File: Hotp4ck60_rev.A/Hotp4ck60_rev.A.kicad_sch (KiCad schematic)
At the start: 42 parts, among them Q1 2N7002, SW1 PWR, U1 nRF52840, U2 BQ24075RGT, U3 TPS7A20xxxDQN, U4 MAX17048, X1 32 MHz, X2 32.768 KHz

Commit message: 기판 아트웍 재시작
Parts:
- U2: footprint Package_DFN_QFN:VQFN-16-1EP_3x3mm_P0.5mm_EP1.6x1.6mm -> lib:VQFN-16-1EP_3x3mm_P0.5mm_EP1.6x1.6mm
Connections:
- net ~{RST}: now reaches U1.AC13 (P0.18/~{RESET})
- net ~{RST}: now also U1.AD12 (P0.17)
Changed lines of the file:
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@@
 	(wire
 		(pts
+			(xy 137.16 96.52) (xy 133.35 96.52)
+		)
+		(stroke
+			(width 0)
+			(type default)
+		)
+	)
+	(wire
+		(pts
 			(xy 222.25 119.38) (xy 223.52 119.38)
 		)
@@
 	(wire
 		(pts
+			(xy 63.5 160.02) (xy 67.31 160.02)
+		)
+		(stroke
+			(width 0)
+			(type default)
+		)
+	)
+	(wire
+		(pts
 			(xy 212.09 92.71) (xy 212.09 93.98)
 		)
@@
 		)
 	)
+	(label "~{RST}"
+		(at 63.5 160.02 0)
+		(effects
+			(font
+				(size 1.27 1.27)
+			)
+			(justify left bottom)
+		)
+	)
 	(label "~{CHG}"
 		(at 248.92 53.34 180)
@@
 		)
 	)
+	(label "~{RST}"
+		(at 137.16 96.52 180)
+		(effects
+			(font
+				(size 1.27 1.27)
+			)
+			(justify right bottom)
+		)
+	)
 	(label "XL1"
 		(at 137.16 53.34 180)
@@
 			)
 		)
-		(property "Footprint" "Package_DFN_QFN:VQFN-16-1EP_3x3mm_P0.5mm_EP1.6x1.6mm"
+		(property "Footprint" "lib:VQFN-16-1EP_3x3mm_P0.5mm_EP1.6x1.6mm"
 			(at 238.76 57.15 0)
 			(hide yes)

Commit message: 키보드 기판 소자 재배치 중
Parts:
- added AE1: ANT, RF_Antenna:Texas_SWRA117D_2.4GHz_Right, symbol Device:Antenna_Dipole
- added C24: 0.8nF, Capacitor_SMD:C_0402_1005Metric, symbol PCM_JLCPCB-Capacitors:0402,100nF,(2)
- added C25: 0.5nF, Capacitor_SMD:C_0402_1005Metric, symbol PCM_JLCPCB-Capacitors:0402,100nF,(2)
- added J1: POGO, Connector_PinHeader_2.54mm:PinHeader_1x05_P2.54mm_Vertical, symbol Connector_Generic:Conn_01x05
- added J2: ai03_unified_daughter_board, Connector_JST:JST_SH_SM04B-SRSS-TB_1x04-1MP_P1.00mm_Horizontal, symbol Connector_Generic_MountingPin:Conn_01x04_MountingPin
- added J3: Battery Connector, Connector_Molex:Molex_PicoBlade_53261-0271_1x02-1MP_P1.25mm_Horizontal, symbol Connector_Generic_MountingPin:Conn_01x02_MountingPin
- added L3: 4.7nH, 700mA, Inductor_SMD:L_0402_1005Metric, symbol Device:L_Small
- added R1: 0Ω, Resistor_SMD:R_0402_1005Metric, symbol PCM_JLCPCB-Resistors:0402,0Ω
- L1: value 10 uH, 50mA -> 10uH,50mA; Category (none) -> Inductors/Coils/Transformers,Inductors (SMD); Class (none) -> Extended Component; DC Resistance (DCR) (none) -> 900mΩ; Inductance (none) -> 10uH; LCSC (none) -> C50325679; Manufacturer (none) -> APV; Part (none) -> APQM18FN100M00D; Process (none) -> SMT; Rated Current (none) -> 50mA; Tolerance (none) -> ±20%
- L2: value 15 nH -> 15nH; Category (none) -> Inductors/Coils/Transformers,Inductors (SMD); Class (none) -> Extended Component; DC Resistance (DCR) (none) -> 500mΩ; Inductance (none) -> 15nH; LCSC (none) -> C395049; Manufacturer (none) -> FH; Part (none) -> VHF100505HQ15NJT; Process (none) -> SMT; Rated Current (none) -> 400mA; Tolerance (none) -> ±5%
- renumbered R1 to R2, R2 to R3, R3 to R4, R4 to R5
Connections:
- net +BATT: now also J1.5 (Pin_5), J3.1 (Pin_1)
- net GND: now also Q1.2 (S), R9.2, SW1.3 (C), AE1.2, C24.1, C25.1, J1.4 (Pin_4), J2.4 (Pin_4), J2.MP (MountPin), J3.2 (Pin_2), J3.MP (MountPin), R1.1
- net SCL: now also U1.U24 (P1.04)
- net SDA: now also U1.W24 (P1.02)
- net VBUS: now also J1.1 (Pin_1), J2.1 (Pin_1)
- net D-: now reaches U1.AD4 (D-)
- net D-: now also J1.2 (Pin_2), J2.2 (Pin_2)
- net D+: now reaches U1.AD6 (D+)
- net D+: now also J1.3 (Pin_3), J2.3 (Pin_3)
- net at U1.H23 (ANT): now also C24.2, L3.2
- new net: AE1.1, C25.2, L3.1, R1.2
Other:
- moved on the sheet: L1, L2

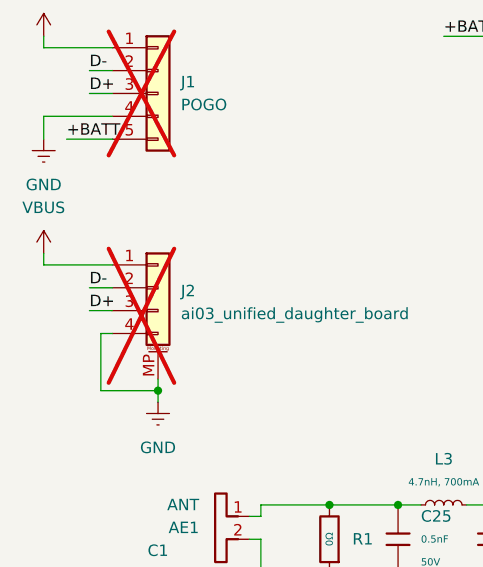
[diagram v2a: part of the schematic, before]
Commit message: 키보드 기판 소자 재배치 중
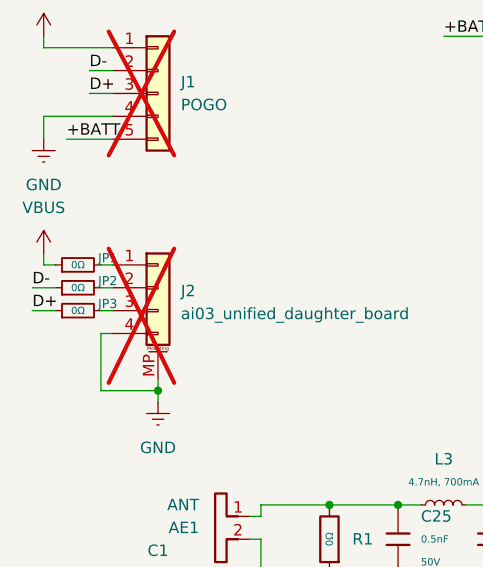
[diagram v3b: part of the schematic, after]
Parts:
- added JP1, JP2, JP3: 0Ω, Resistor_SMD:R_0201_0603Metric, symbol Device:R_Small
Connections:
- net D+: now also JP3.1; no longer J2.3 (Pin_3)
- net D-: now also JP2.1; no longer J2.2 (Pin_2)
- net VBUS: now also JP1.1; no longer J2.1 (Pin_1)
- new net: J2.2 (Pin_2), JP2.2
- new net: J2.1 (Pin_1), JP1.2
- new net: J2.3 (Pin_3), JP3.2
